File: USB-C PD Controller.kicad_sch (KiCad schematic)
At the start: 20 parts, among them U10 TPS25751DREFR

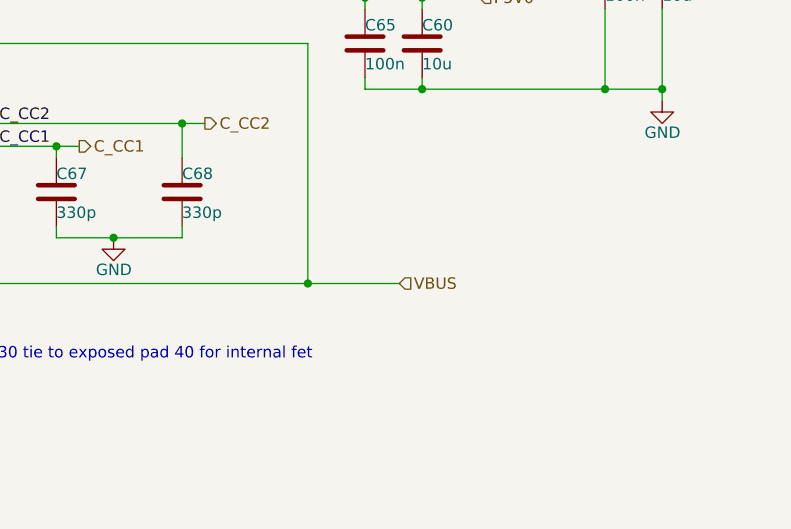
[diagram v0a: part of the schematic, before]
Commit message: Fixed 5V Line
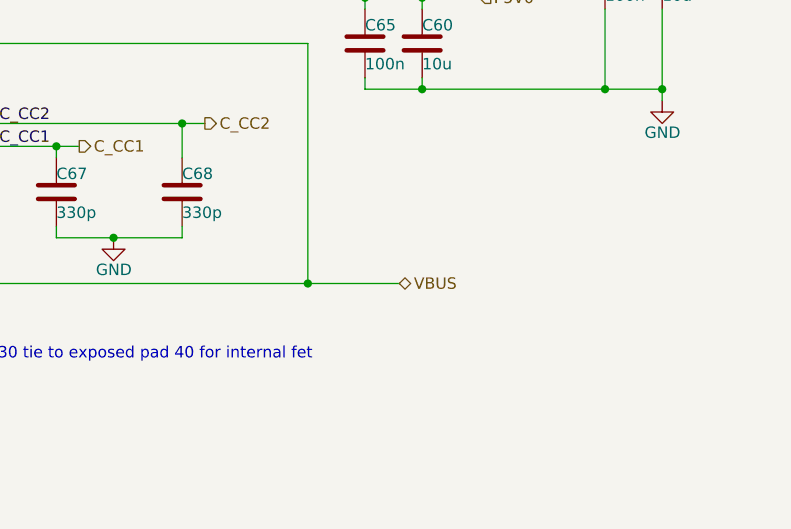
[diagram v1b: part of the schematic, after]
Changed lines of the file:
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@@
 	)
 	(hierarchical_label "VBUS"
-		(shape input)
+		(shape bidirectional)
 		(at 223.52 118.11 0)
 		(effects
